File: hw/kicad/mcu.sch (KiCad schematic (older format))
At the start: 43 parts, among them P1 CONN_01X06, P2 CONN_01X03, P3 CONN_02X05, P4 CONN_01X05, SW1 PTS810, U1 STM32F446R(C-E)Tx, Y1 16 MHz

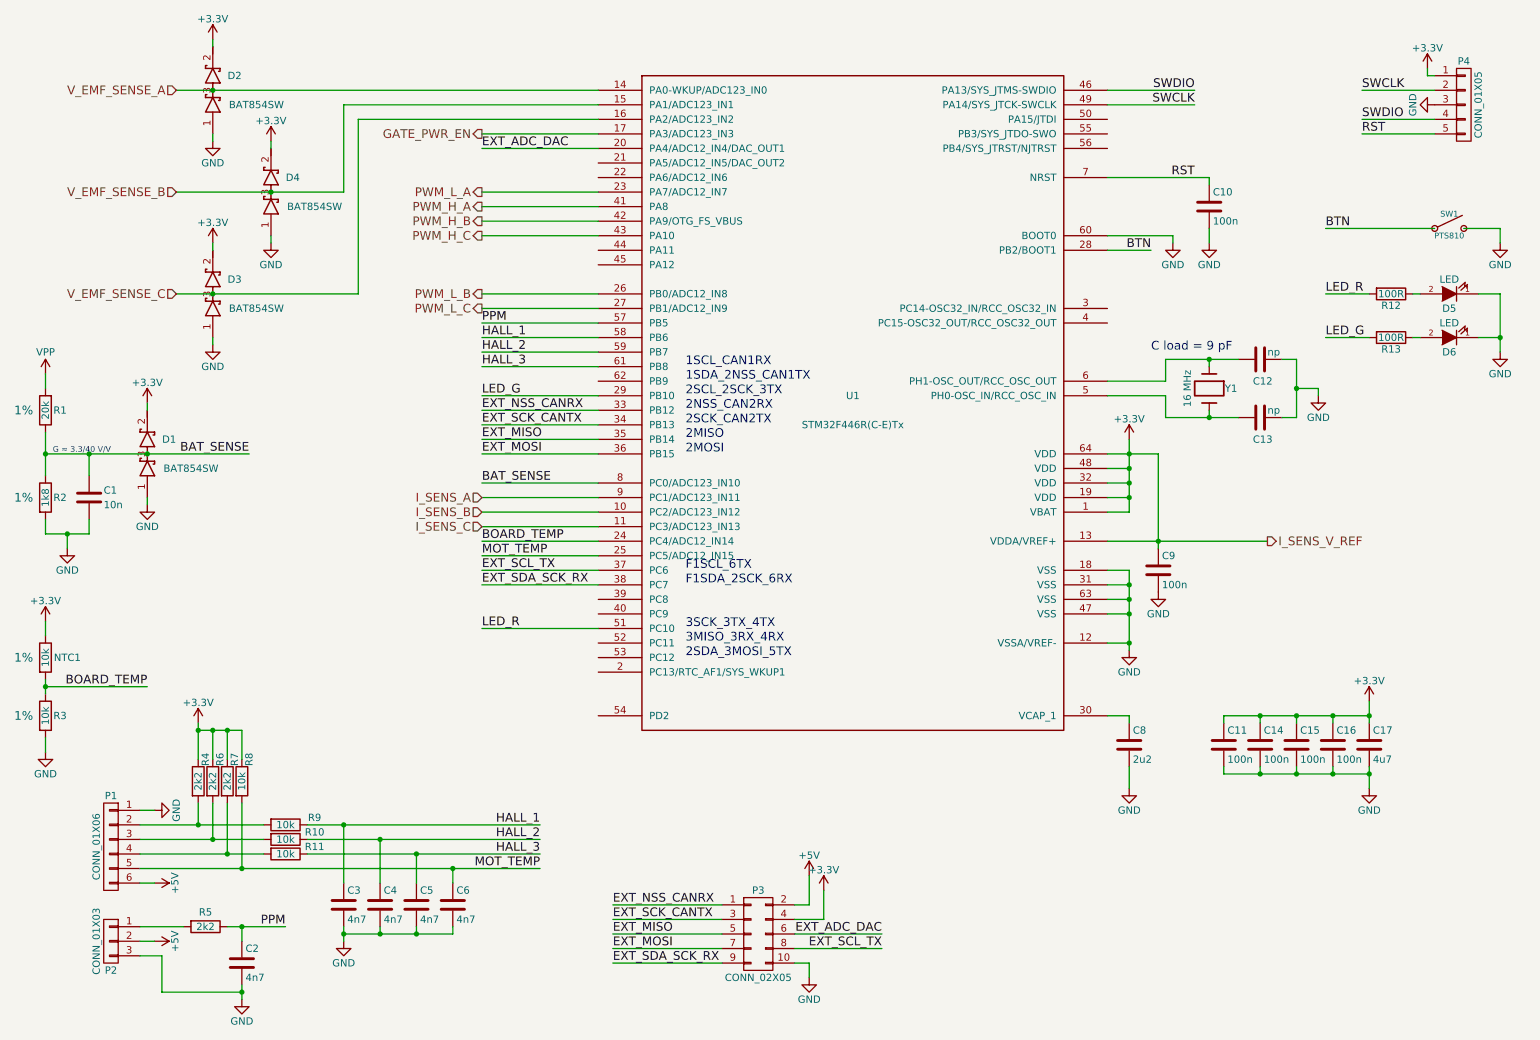
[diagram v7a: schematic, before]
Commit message: Added current sense voltage reference as reparate net again
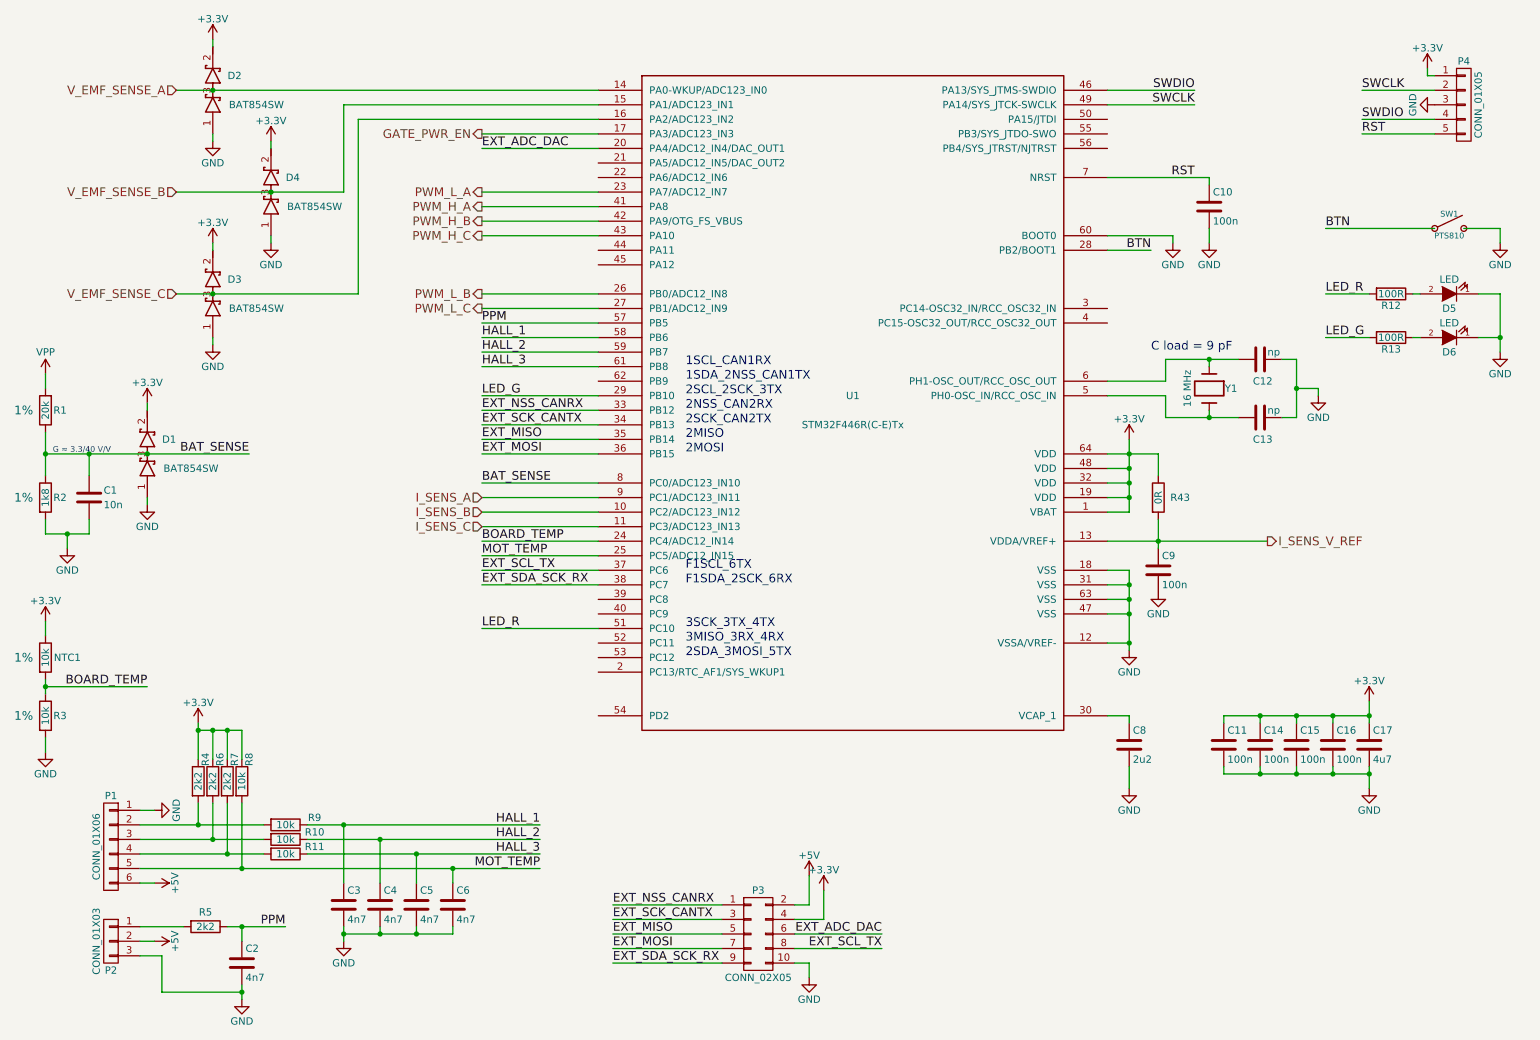
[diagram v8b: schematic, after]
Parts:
- added R43: 0R, Resistors_SMD:R_0402, symbol R
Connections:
- net +3V3: now also R43.1; no longer C9.1, U1.13 (VDDA/VREF+)
- new net I_SENS_V_REF: C9.1, R43.2, U1.13 (VDDA/VREF+)
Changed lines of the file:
@@
 $EndComp
 $Comp
-L +3.3V #PWR01
+L +3.3V #PWR29
 U 1 1 5815B255
 P 10000 5500
-F 0 "#PWR01" H 10000 5350 50  0001 C CNN
+F 0 "#PWR29" H 10000 5350 50  0001 C CNN
 F 1 "+3.3V" H 10000 5640 50  0000 C CNN
 F 2 "" H 10000 5500 60  0000 C CNN
@@
 $EndComp
 $Comp
-L +3.3V #PWR02
+L +3.3V #PWR22
 U 1 1 5815B2D5
 P 8350 3700
-F 0 "#PWR02" H 8350 3550 50  0001 C CNN
+F 0 "#PWR22" H 8350 3550 50  0001 C CNN
 F 1 "+3.3V" H 8350 3840 50  0000 C CNN
 F 2 "" H 8350 3700 60  0000 C CNN
@@
 $EndComp
 $Comp
-L +3.3V #PWR03
+L +3.3V #PWR5
 U 1 1 5821B0F1
 P 1600 3450
-F 0 "#PWR03" H 1600 3300 50  0001 C CNN
+F 0 "#PWR5" H 1600 3300 50  0001 C CNN
 F 1 "+3.3V" H 1600 3590 50  0000 C CNN
 F 2 "" H 1600 3450 60  0000 C CNN
@@
 $EndComp
 $Comp
-L +3.3V #PWR04
+L +3.3V #PWR13
 U 1 1 5821BAD6
 P 2050 2350
-F 0 "#PWR04" H 2050 2200 50  0001 C CNN
+F 0 "#PWR13" H 2050 2200 50  0001 C CNN
 F 1 "+3.3V" H 2050 2490 50  0000 C CNN
 F 2 "" H 2050 2350 60  0000 C CNN
@@
 $EndComp
 $Comp
-L +3.3V #PWR05
+L +3.3V #PWR16
 U 1 1 5821C068
 P 2450 1650
-F 0 "#PWR05" H 2450 1500 50  0001 C CNN
+F 0 "#PWR16" H 2450 1500 50  0001 C CNN
 F 1 "+3.3V" H 2450 1790 50  0000 C CNN
 F 2 "" H 2450 1650 60  0000 C CNN
@@
 $EndComp
 $Comp
-L +3.3V #PWR06
+L +3.3V #PWR11
 U 1 1 5821C7C9
 P 2050 950
-F 0 "#PWR06" H 2050 800 50  0001 C CNN
+F 0 "#PWR11" H 2050 800 50  0001 C CNN
 F 1 "+3.3V" H 2050 1090 50  0000 C CNN
 F 2 "" H 2050 950 60  0000 C CNN
@@
 $EndComp
 $Comp
-L +5V #PWR07
+L +5V #PWR8
 U 1 1 5823D67C
 P 1650 6750
-F 0 "#PWR07" H 1650 6600 50  0001 C CNN
+F 0 "#PWR8" H 1650 6600 50  0001 C CNN
 F 1 "+5V" H 1650 6890 50  0000 C CNN
 F 2 "" H 1650 6750 60  0000 C CNN
@@
 Wire Wire Line
 	8200 4400 9300 4400
-Wire Wire Line
-	8550 3800 8550 4450
 Connection ~ 8550 4400
 Wire Wire Line
@@
 	4700 1400 2950 1400
 Wire Wire Line
-	2950 2000 2950 1400
-Wire Wire Line
-	1800 2000 2950 2000
+	2950 1400 2950 2000
+Wire Wire Line
+	2950 2000 1800 2000
 Wire Wire Line
 	3050 2700 3050 1500
@@
 Connection ~ 2950 7100
 $Comp
-L +3.3V #PWR08
+L +3.3V #PWR10
 U 1 1 5823F97D
 P 1950 5650
-F 0 "#PWR08" H 1950 5500 50  0001 C CNN
+F 0 "#PWR10" H 1950 5500 50  0001 C CNN
 F 1 "+3.3V" H 1950 5790 50  0000 C CNN
 F 2 "" H 1950 5650 60  0000 C CNN
@@
 HALL_3
 $Comp
-L GND #PWR09
+L GND #PWR12
 U 1 1 5827704E
 P 2050 1650
-F 0 "#PWR09" H 2050 1400 50  0001 C CNN
+F 0 "#PWR12" H 2050 1400 50  0001 C CNN
 F 1 "GND" H 2050 1500 50  0000 C CNN
 F 2 "" H 2050 1650 60  0000 C CNN
@@
 $EndComp
 $Comp
-L GND #PWR010
+L GND #PWR17
 U 1 1 58277258
 P 2450 2350
-F 0 "#PWR010" H 2450 2100 50  0001 C CNN
+F 0 "#PWR17" H 2450 2100 50  0001 C CNN
 F 1 "GND" H 2450 2200 50  0000 C CNN
 F 2 "" H 2450 2350 60  0000 C CNN
@@
 $EndComp
 $Comp
-L GND #PWR011
+L GND #PWR14
 U 1 1 582772CC
 P 2050 3050
-F 0 "#PWR011" H 2050 2800 50  0001 C CNN
+F 0 "#PWR14" H 2050 2800 50  0001 C CNN
 F 1 "GND" H 2050 2900 50  0000 C CNN
 F 2 "" H 2050 3050 60  0000 C CNN
@@
 $EndComp
 $Comp
-L GND #PWR012
+L GND #PWR6
 U 1 1 58277340
 P 1600 4150
-F 0 "#PWR012" H 1600 3900 50  0001 C CNN
+F 0 "#PWR6" H 1600 3900 50  0001 C CNN
 F 1 "GND" H 1600 4000 50  0000 C CNN
 F 2 "" H 1600 4150 60  0000 C CNN
@@
 $EndComp
 $Comp
-L GND #PWR013
+L GND #PWR18
 U 1 1 582774EF
 P 2950 7150
-F 0 "#PWR013" H 2950 6900 50  0001 C CNN
+F 0 "#PWR18" H 2950 6900 50  0001 C CNN
 F 1 "GND" H 2950 7000 50  0000 C CNN
 F 2 "" H 2950 7150 60  0000 C CNN
@@
 $EndComp
 $Comp
-L GND #PWR014
+L GND #PWR7
 U 1 1 58277759
 P 1650 6250
-F 0 "#PWR014" H 1650 6000 50  0001 C CNN
+F 0 "#PWR7" H 1650 6000 50  0001 C CNN
 F 1 "GND" H 1650 6100 50  0000 C CNN
 F 2 "" H 1650 6250 60  0000 C CNN
@@
 $EndComp
 $Comp
-L GND #PWR015
+L GND #PWR30
 U 1 1 582779AA
 P 10000 6100
-F 0 "#PWR015" H 10000 5850 50  0001 C CNN
+F 0 "#PWR30" H 10000 5850 50  0001 C CNN
 F 1 "GND" H 10000 5950 50  0000 C CNN
 F 2 "" H 10000 6100 60  0000 C CNN
@@
 $EndComp
 $Comp
-L GND #PWR016
+L GND #PWR24
 U 1 1 58277BF1
 P 8350 6100
-F 0 "#PWR016" H 8350 5850 50  0001 C CNN
+F 0 "#PWR24" H 8350 5850 50  0001 C CNN
 F 1 "GND" H 8350 5950 50  0000 C CNN
 F 2 "" H 8350 6100 60  0000 C CNN
@@
 $EndComp
 $Comp
-L GND #PWR017
+L GND #PWR23
 U 1 1 58277C89
 P 8350 5150
-F 0 "#PWR017" H 8350 4900 50  0001 C CNN
+F 0 "#PWR23" H 8350 4900 50  0001 C CNN
 F 1 "GND" H 8350 5000 50  0000 C CNN
 F 2 "" H 8350 5150 60  0000 C CNN
@@
 $EndComp
 $Comp
-L GND #PWR018
+L GND #PWR25
 U 1 1 58277D21
 P 8550 4750
-F 0 "#PWR018" H 8550 4500 50  0001 C CNN
+F 0 "#PWR25" H 8550 4500 50  0001 C CNN
 F 1 "GND" H 8550 4600 50  0000 C CNN
 F 2 "" H 8550 4750 60  0000 C CNN
@@
 $EndComp
 $Comp
-L GND #PWR019
+L GND #PWR28
 U 1 1 58277E8B
 P 9650 3400
-F 0 "#PWR019" H 9650 3150 50  0001 C CNN
+F 0 "#PWR28" H 9650 3150 50  0001 C CNN
 F 1 "GND" H 9650 3250 50  0000 C CNN
 F 2 "" H 9650 3400 60  0000 C CNN
@@
 $EndComp
 $Comp
-L GND #PWR020
+L GND #PWR26
 U 1 1 58277FF6
 P 8650 2350
-F 0 "#PWR020" H 8650 2100 50  0001 C CNN
+F 0 "#PWR26" H 8650 2100 50  0001 C CNN
 F 1 "GND" H 8650 2200 50  0000 C CNN
 F 2 "" H 8650 2350 60  0000 C CNN
@@
 $EndComp
 $Comp
-L GND #PWR021
+L GND #PWR27
 U 1 1 5827806A
 P 8900 2350
-F 0 "#PWR021" H 8900 2100 50  0001 C CNN
+F 0 "#PWR27" H 8900 2100 50  0001 C CNN
 F 1 "GND" H 8900 2200 50  0000 C CNN
 F 2 "" H 8900 2350 60  0000 C CNN
@@
 $EndComp
 $Comp
-L VPP #PWR022
+L VPP #PWR1
 U 1 1 582916A9
 P 900 3250
-F 0 "#PWR022" H 900 3100 50  0001 C CNN
+F 0 "#PWR1" H 900 3100 50  0001 C CNN
 F 1 "VPP" H 900 3400 50  0000 C CNN
 F 2 "" H 900 3250 60  0000 C CNN
@@
 	900  4250 900  4350
 $Comp
-L GND #PWR023
+L GND #PWR4
 U 1 1 582916B5
 P 1050 4450
-F 0 "#PWR023" H 1050 4200 50  0001 C CNN
+F 0 "#PWR4" H 1050 4200 50  0001 C CNN
 F 1 "GND" H 1050 4300 50  0000 C CNN
 F 2 "" H 1050 4450 60  0000 C CNN
@@
 $EndComp
 $Comp
-L +3.3V #PWR024
+L +3.3V #PWR2
 U 1 1 5833D72B
 P 900 4950
-F 0 "#PWR024" H 900 4800 50  0001 C CNN
+F 0 "#PWR2" H 900 4800 50  0001 C CNN
 F 1 "+3.3V" H 900 5090 50  0000 C CNN
 F 2 "" H 900 4950 60  0000 C CNN
@@
 	900  5050 900  4950
 $Comp
-L GND #PWR025
+L GND #PWR3
 U 1 1 5833D8AB
 P 900 5850
-F 0 "#PWR025" H 900 5600 50  0001 C CNN
+F 0 "#PWR3" H 900 5600 50  0001 C CNN
 F 1 "GND" H 900 5700 50  0000 C CNN
 F 2 "" H 900 5850 60  0000 C CNN
@@
 Connection ~ 10900 3000
 $Comp
-L GND #PWR026
+L GND #PWR34
 U 1 1 58363604
 P 10900 3100
-F 0 "#PWR026" H 10900 2850 50  0001 C CNN
+F 0 "#PWR34" H 10900 2850 50  0001 C CNN
 F 1 "GND" H 10900 2950 50  0000 C CNN
 F 2 "" H 10900 3100 60  0000 C CNN
@@
 $EndComp
 $Comp
-L +5V #PWR027
+L +5V #PWR9
 U 1 1 58398559
 P 1650 7150
-F 0 "#PWR027" H 1650 7000 50  0001 C CNN
+F 0 "#PWR9" H 1650 7000 50  0001 C CNN
 F 1 "+5V" H 1650 7290 50  0000 C CNN
 F 2 "" H 1650 7150 60  0000 C CNN
@@
 	2250 7050 2250 7150
 $Comp
-L GND #PWR028
+L GND #PWR15
 U 1 1 58399288
 P 2250 7550
-F 0 "#PWR028" H 2250 7300 50  0001 C CNN
+F 0 "#PWR15" H 2250 7300 50  0001 C CNN
 F 1 "GND" H 2250 7400 50  0000 C CNN
 F 2 "" H 2250 7550 60  0000 C CNN
@@
 $EndComp
 $Comp
-L +3.3V #PWR029
+L +3.3V #PWR21
 U 1 1 5839AEF9
 P 6250 6800
-F 0 "#PWR029" H 6250 6650 50  0001 C CNN
+F 0 "#PWR21" H 6250 6650 50  0001 C CNN
 F 1 "+3.3V" H 6250 6940 50  0000 C CNN
 F 2 "" H 6250 6800 60  0000 C CNN
@@
 $EndComp
 $Comp
-L GND #PWR030
+L GND #PWR20
 U 1 1 5839AF82
 P 6150 7400
-F 0 "#PWR030" H 6150 7150 50  0001 C CNN
+F 0 "#PWR20" H 6150 7150 50  0001 C CNN
 F 1 "GND" H 6150 7250 50  0000 C CNN
 F 2 "" H 6150 7400 60  0000 C CNN
@@
 $EndComp
 $Comp
-L +5V #PWR031
+L +5V #PWR19
 U 1 1 5839B00B
 P 6150 6700
-F 0 "#PWR031" H 6150 6550 50  0001 C CNN
+F 0 "#PWR19" H 6150 6550 50  0001 C CNN
 F 1 "+5V" H 6150 6840 50  0000 C CNN
 F 2 "" H 6150 6700 60  0000 C CNN
@@
 $EndComp
 $Comp
-L GND #PWR032
+L GND #PWR33
 U 1 1 583BE21E
 P 10900 2350
-F 0 "#PWR032" H 10900 2100 50  0001 C CNN
+F 0 "#PWR33" H 10900 2100 50  0001 C CNN
 F 1 "GND" H 10900 2200 50  0000 C CNN
 F 2 "" H 10900 2350 60  0000 C CNN
@@
 BTN
 $Comp
-L GND #PWR033
+L GND #PWR32
 U 1 1 5842C05B
 P 10450 1400
-F 0 "#PWR033" H 10450 1150 50  0001 C CNN
+F 0 "#PWR32" H 10450 1150 50  0001 C CNN
 F 1 "GND" H 10450 1250 50  0000 C CNN
 F 2 "" H 10450 1400 60  0000 C CNN
@@
 $EndComp
 $Comp
-L +3.3V #PWR034
+L +3.3V #PWR31
 U 1 1 5842C60A
 P 10400 1150
-F 0 "#PWR034" H 10400 1000 50  0001 C CNN
+F 0 "#PWR31" H 10400 1000 50  0001 C CNN
 F 1 "+3.3V" H 10400 1290 50  0000 C CNN
 F 2 "" H 10400 1150 60  0000 C CNN
@@
 Wire Wire Line
 	8500 2400 8200 2400
+$Comp
+L R R43
+U 1 1 58567422
+P 8550 4100
+F 0 "R43" H 8700 4100 50  0000 C CNN
+F 1 "0R" V 8550 4100 50  0000 C CNN
+F 2 "Resistors_SMD:R_0402" V 8480 4100 30  0001 C CNN
+F 3 "" H 8550 4100 30  0000 C CNN
+	1    8550 4100
+	1    0    0    -1
+$EndComp
+Wire Wire Line
+	8550 3800 8550 3950
+Wire Wire Line
+	8550 4250 8550 4450
 $EndSCHEMATC
